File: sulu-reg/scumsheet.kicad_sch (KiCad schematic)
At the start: 19 parts

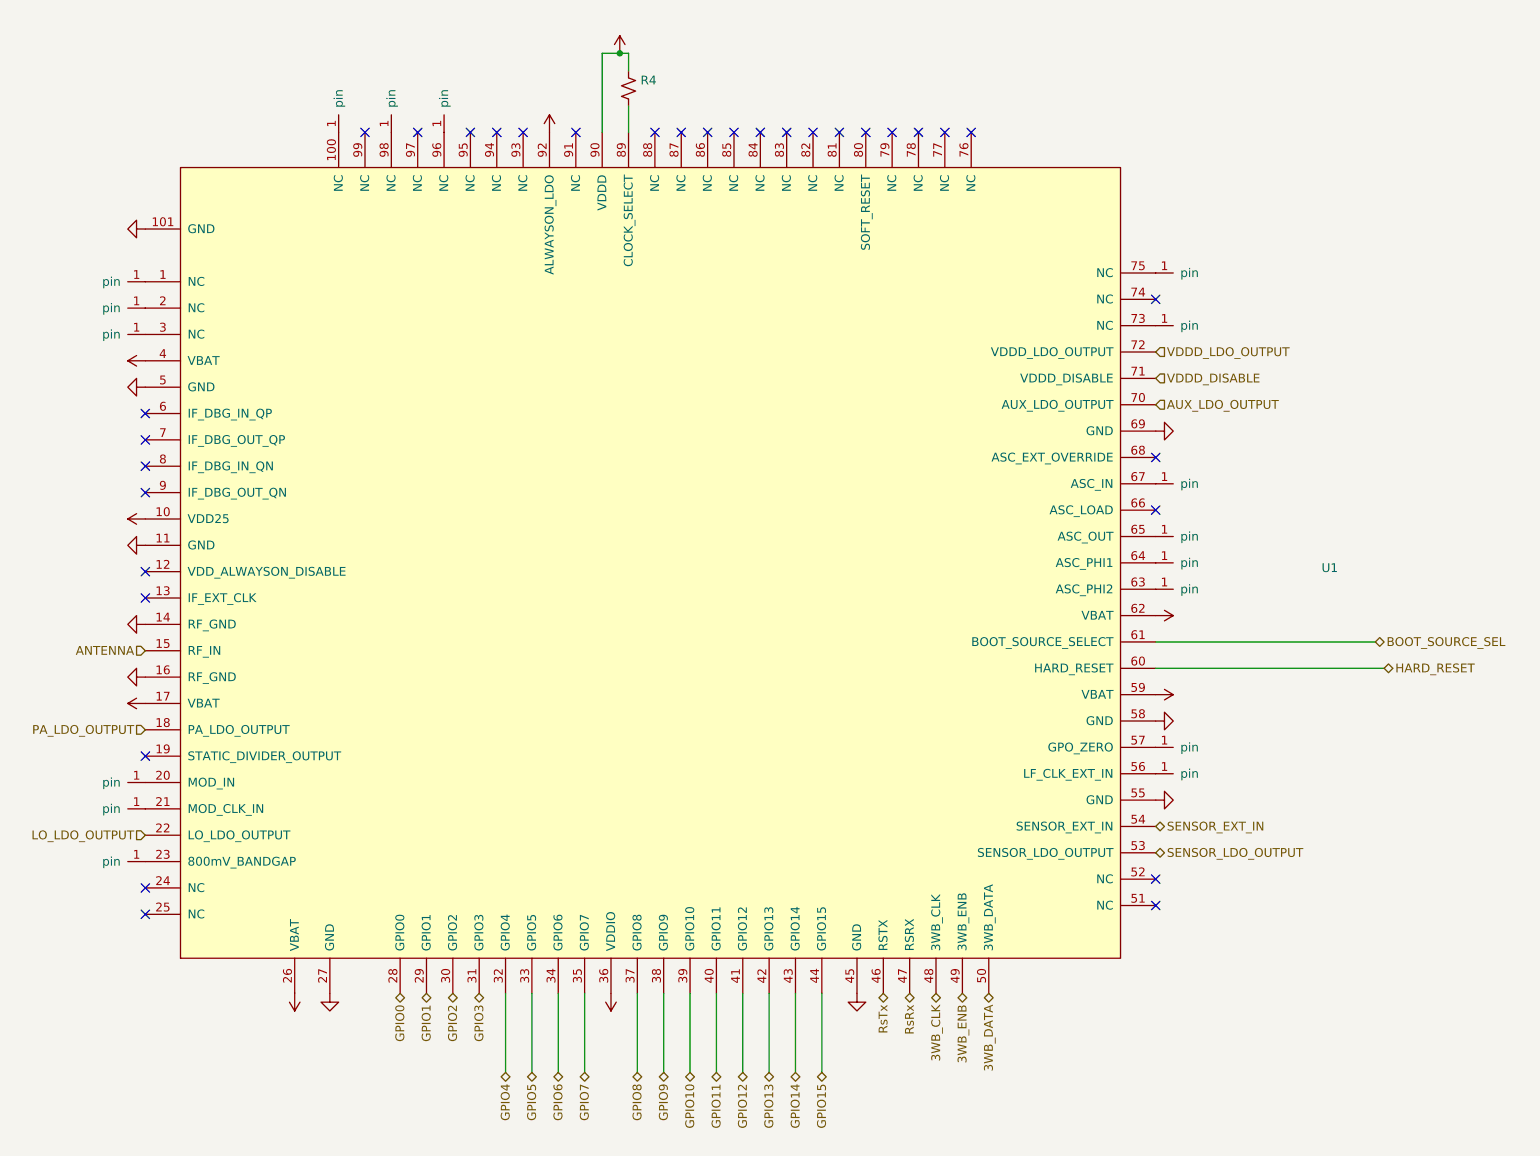
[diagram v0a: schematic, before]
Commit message: Re-order 3WB header locations
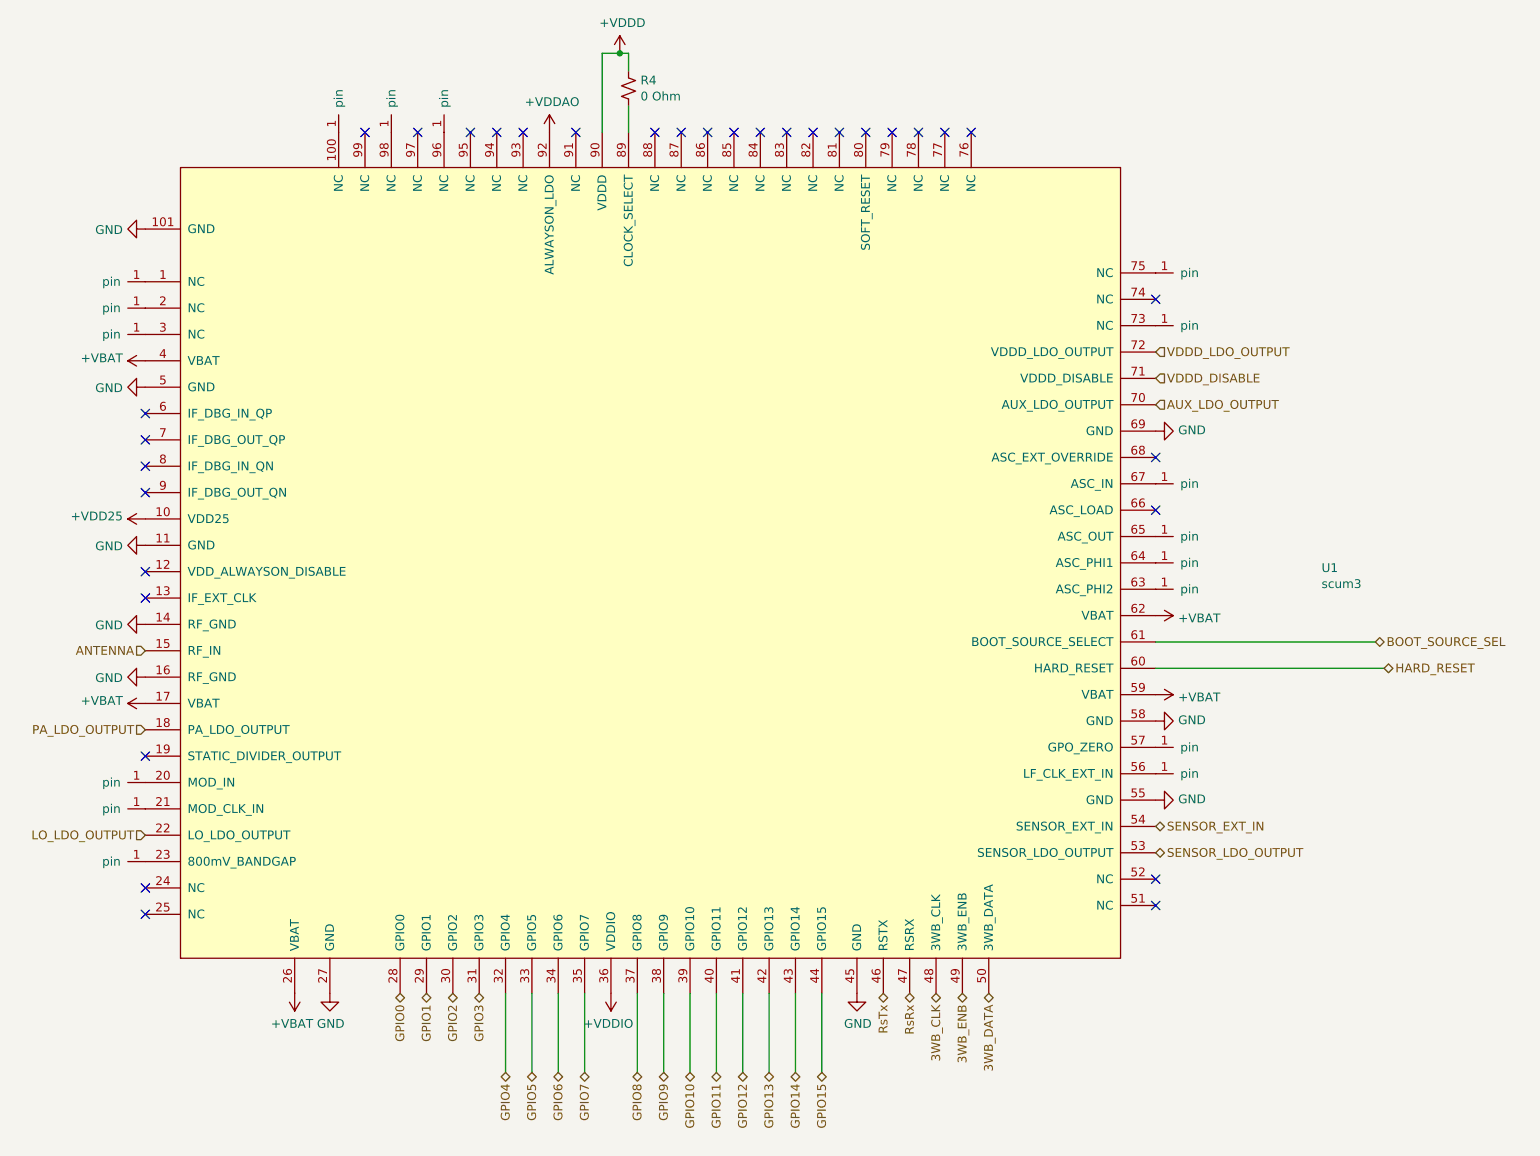
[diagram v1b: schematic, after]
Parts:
- J10, J11, J12, J13, J14, J15, J16, J17, J18, J19, J20, J21, J5, J6, J7, J8, J9: value (none) -> through_hole; footprint (none) -> SCUM:through_hole
- R4: value (none) -> 0 Ohm; footprint (none) -> Resistor_SMD:R_0402_1005Metric
- U1: value (none) -> scum3; footprint (none) -> SCUM:QFN-100_EP_12x12_Pitch0.4mm_Margin0.25mm
